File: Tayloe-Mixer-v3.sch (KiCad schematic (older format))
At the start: 61 parts, among them J1 BNC, J101 Audio_Jack, J2 Conn_01x04, J3 Pad, J4 Conn_01x07_Female, J5 Pad, Q1 2N3904-SMD, Q2 2N3904-SMD, SW1 SW_DIP_x01, SW2 Rotary_Encoder_Switch, T1 6:31, T2 31:6, T3 T50_SPLITTER, U1 ESP32-A1S, U2 FST3253, U201 MAR6, U3 LM4562, U4 si5351, U5 L7805, U7 AMS1117CD-3.3

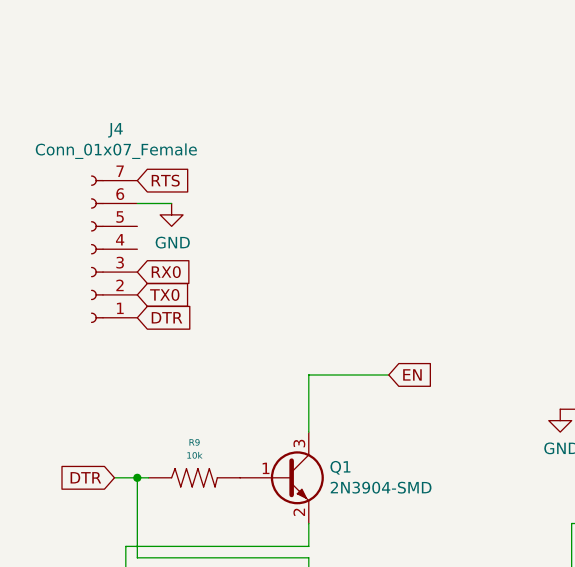
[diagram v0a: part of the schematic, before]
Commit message: fixed rx/tx
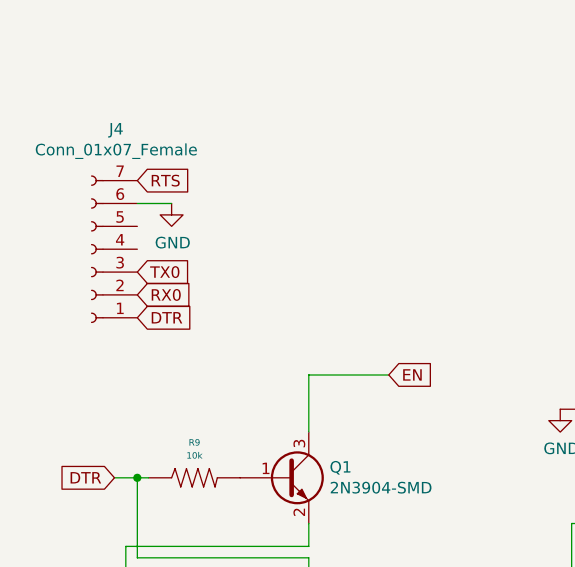
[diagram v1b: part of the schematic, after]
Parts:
- removed U1: ESP32-A1S, xenir:ESP32-A1S, symbol Tayloe-Mixer-v3-rescue:ESP32-A1S-xenir
- added U1: ESP32-A1S, Xenir:ESP32-A1S, symbol xenir:ESP32-A1S
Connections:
- net +3V3: now also U1.2 (3V3)
- net EN: now also U1.35 (EN)
- net GND: now also U1.1 (GND), U1.19 (GND), U1.20 (GND), U1.38 (GND)
- net IO0: now also U1.6 (IO0)
- net OUTL: now also U1.27 (HPOUTL)
- net OUTR: now also U1.28 (HPOUTR)
- net RX0: now also J4.2 (Pin_2), U1.36 (TXD0); no longer J4.3 (Pin_3)
- net SCL: now also U1.32 (IO19)
- net SDA: now also U1.31 (IO23)
- net TX0: now also J4.3 (Pin_3), U1.37 (RXD0); no longer J4.2 (Pin_2)
- net at SW2.A: now also U1.10 (IO15)
- net at SW2.S2: now also U1.12 (IO4)
- net at C104.2: now also U1.21 (LINEINR)
- net at C103.2: now also U1.22 (LINEINL)
- net at SW2.B: now also U1.8 (IO12)
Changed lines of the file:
@@
 EndData
 $EndBitmap
-$Comp
-L Tayloe-Mixer-v3-rescue:ESP32-A1S-xenir U1
-U 1 1 62B0B8E9
-P 5950 8450
-F 0 "U1" H 5950 9707 50  0000 C CNN
-F 1 "ESP32-A1S" H 5950 9616 50  0000 C CNN
-F 2 "xenir:ESP32-A1S" H 5350 9650 50  0001 L BNN
-F 3 "" H 5950 9500 50  0001 L BNN
-F 4 "4" H 5950 9525 50  0000 C CNN "PARTREV"
-F 5 "Espressif Systems" H 5550 9600 50  0001 L BNN "MANUFACTURER"
-	1    5950 8450
-	1    0    0    -1
-$EndComp
 Text GLabel 6750 7850 2    50   Input ~ 0
 EN
@@
 Text GLabel 1500 7200 2    50   Input ~ 0
 DTR
-Text GLabel 1500 7100 2    50   Input ~ 0
-TX0
 Text GLabel 1500 7000 2    50   Input ~ 0
+TX0
+Text GLabel 1500 7100 2    50   Input ~ 0
 RX0
 $Comp
@@
 EndData
 $EndBitmap
+$Comp
+L xenir:ESP32-A1S U1
+U 1 1 6363210B
+P 5950 8450
+F 0 "U1" H 5950 9707 50  0000 C CNN
+F 1 "ESP32-A1S" H 5950 9616 50  0000 C CNN
+F 2 "Xenir:ESP32-A1S" H 5350 9650 50  0001 L BNN
+F 3 "" H 5950 9500 50  0001 L BNN
+F 4 "4" H 5950 9525 50  0000 C CNN "PARTREV"
+F 5 "Espressif Systems" H 5550 9600 50  0001 L BNN "MANUFACTURER"
+	1    5950 8450
+	1    0    0    -1
+$EndComp
 $EndSCHEMATC

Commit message: gg
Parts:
- C203: symbol preamp-mar6-rescue:Capacitor-xenir -> Tayloe-Mixer-v3-rescue:Capacitor-xenir-preamp-mar6-rescue
- C204: symbol preamp-mar6-rescue:Cap_Polarized-xenir -> Tayloe-Mixer-v3-rescue:Cap_Polarized-xenir-preamp-mar6-rescue
- L201: symbol preamp-mar6-rescue:Inductor-xenir -> Tayloe-Mixer-v3-rescue:Inductor-xenir-preamp-mar6-rescue
- R201: symbol preamp-mar6-rescue:Resistor-xenir -> Tayloe-Mixer-v3-rescue:Resistor-xenir-preamp-mar6-rescue
- U1: symbol xenir:ESP32-A1S -> Tayloe-Mixer-v3-rescue:ESP32-A1S-xenir
- U201: symbol preamp-mar6-rescue:MAR6-xenir -> Tayloe-Mixer-v3-rescue:MAR6-xenir-preamp-mar6-rescue
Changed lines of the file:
@@
 Connection ~ 7050 2650
 $Comp
-L preamp-mar6-rescue:Inductor-xenir L201
+L Tayloe-Mixer-v3-rescue:Inductor-xenir-preamp-mar6-rescue L201
 U 1 1 62D06805
 P 7050 2100
@@
 $EndComp
 $Comp
-L preamp-mar6-rescue:Resistor-xenir R201
+L Tayloe-Mixer-v3-rescue:Resistor-xenir-preamp-mar6-rescue R201
 U 1 1 62D0720F
 P 7050 1600
@@
 $EndComp
 $Comp
-L preamp-mar6-rescue:Capacitor-xenir C203
+L Tayloe-Mixer-v3-rescue:Capacitor-xenir-preamp-mar6-rescue C203
 U 1 1 62D08B85
 P 7600 1550
@@
 $EndComp
 $Comp
-L preamp-mar6-rescue:Cap_Polarized-xenir C204
+L Tayloe-Mixer-v3-rescue:Cap_Polarized-xenir-preamp-mar6-rescue C204
 U 1 1 62D09564
 P 8150 1550
@@
 $EndComp
 $Comp
-L preamp-mar6-rescue:MAR6-xenir U201
+L Tayloe-Mixer-v3-rescue:MAR6-xenir-preamp-mar6-rescue U201
 U 1 1 62D05110
 P 6650 2550
@@
 $EndBitmap
 $Comp
-L xenir:ESP32-A1S U1
+L Tayloe-Mixer-v3-rescue:ESP32-A1S-xenir U1
 U 1 1 6363210B
 P 5950 8450
